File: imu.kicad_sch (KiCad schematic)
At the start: 9 parts, among them U5 MPU-6500

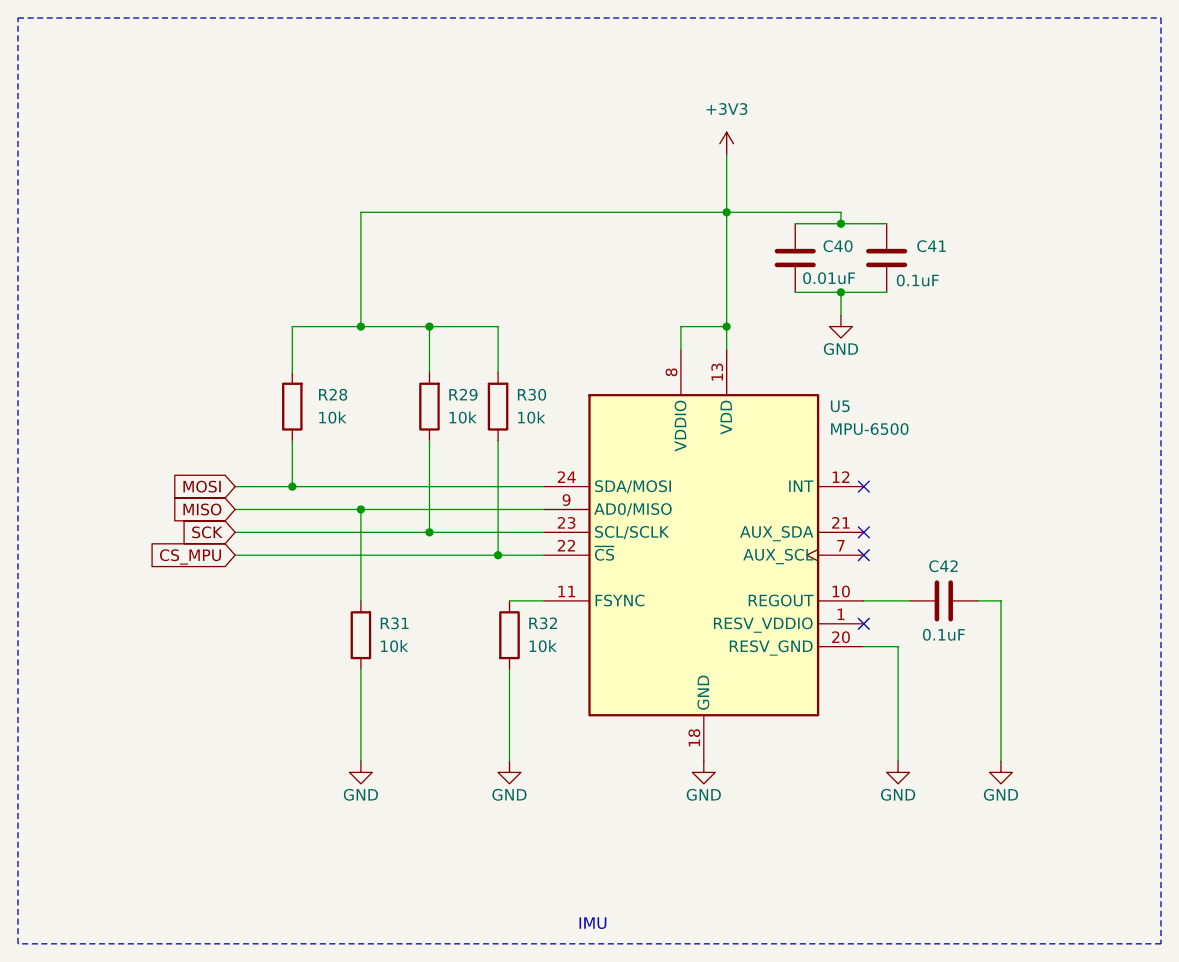
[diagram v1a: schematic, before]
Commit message: Major update on results of testing first order board and on results of crosscheck
* reworked mainswitch scheme
* mainswitch divider. expected commutation time - 2us
* added 3v3bt and 3v3hall
* tvs on hall
* divided 5vhall, 3vhall, 3vbt
* fix misplacement gnd and 3v3 at the BT connector
* fix motorbut (now pullup and gnd on button)
* fix opto gate

+ a lot of minors
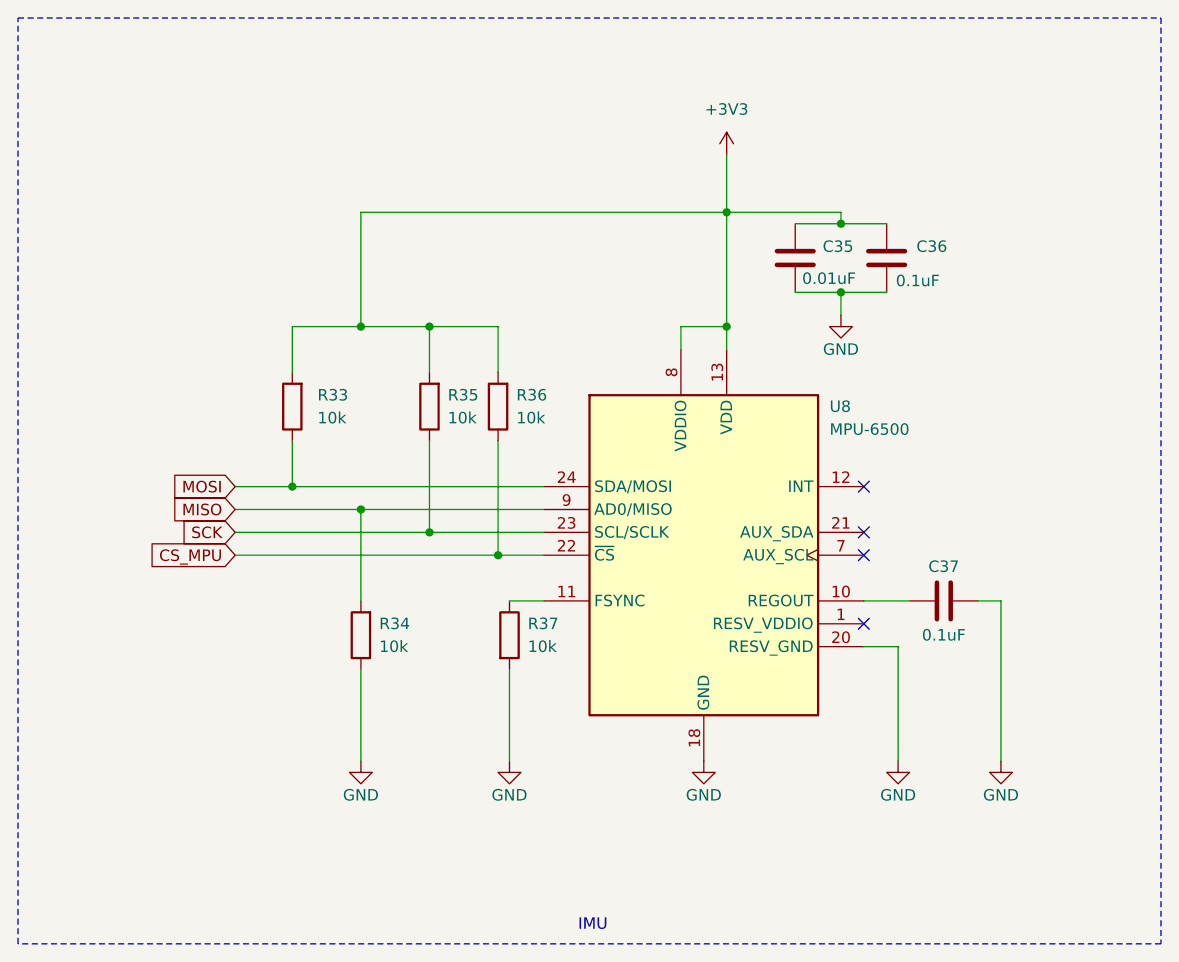
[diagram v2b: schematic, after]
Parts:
- renumbered C40 to C35, C41 to C36, C42 to C37, R28 to R33, R31 to R34, R29 to R35, R30 to R36, R32 to R37, U5 to U8
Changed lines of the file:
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@@
 		(on_board yes)
 		(dnp no)
-		(property "Reference" "R32"
+		(property "Reference" "R37"
 			(at 145.542 113.0299 0)
 			(effects
@@
 			(project "ShiftWay_f103"
 				(path "/c57bc97c-1c43-4bb1-9424-fed846030b7b/44aacc1d-3f92-4714-b852-d77f581a6611"
-					(reference "R32")
+					(reference "R37")
 					(unit 1)
 				)
@@
 		(on_board yes)
 		(dnp no)
-		(property "Reference" "#PWR074"
+		(property "Reference" "#PWR073"
 			(at 186.69 134.62 0)
 			(effects
@@
 			(project "ShiftWay_f103"
 				(path "/c57bc97c-1c43-4bb1-9424-fed846030b7b/44aacc1d-3f92-4714-b852-d77f581a6611"
-					(reference "#PWR074")
+					(reference "#PWR073")
 					(unit 1)
 				)
@@
 		(dnp no)
 		(fields_autoplaced yes)
-		(property "Reference" "#PWR069"
+		(property "Reference" "#PWR071"
 			(at 167.64 64.77 0)
 			(effects
@@
 			(project "ShiftWay_f103"
 				(path "/c57bc97c-1c43-4bb1-9424-fed846030b7b/44aacc1d-3f92-4714-b852-d77f581a6611"
-					(reference "#PWR069")
+					(reference "#PWR071")
 					(unit 1)
 				)
@@
 		(on_board yes)
 		(dnp no)
-		(property "Reference" "C41"
+		(property "Reference" "C36"
 			(at 188.722 71.1199 0)
 			(effects
@@
 			(project "ShiftWay_f103"
 				(path "/c57bc97c-1c43-4bb1-9424-fed846030b7b/44aacc1d-3f92-4714-b852-d77f581a6611"
-					(reference "C41")
+					(reference "C36")
 					(unit 1)
 				)
@@
 		(dnp no)
 		(fields_autoplaced yes)
-		(property "Reference" "R29"
+		(property "Reference" "R35"
 			(at 136.652 87.6299 0)
 			(effects
@@
 			(project "ShiftWay_f103"
 				(path "/c57bc97c-1c43-4bb1-9424-fed846030b7b/44aacc1d-3f92-4714-b852-d77f581a6611"
-					(reference "R29")
+					(reference "R35")
 					(unit 1)
 				)
@@
 		(on_board yes)
 		(dnp no)
-		(property "Reference" "#PWR073"
+		(property "Reference" "#PWR070"
 			(at 165.1 134.62 0)
 			(effects
@@
 			(project "ShiftWay_f103"
 				(path "/c57bc97c-1c43-4bb1-9424-fed846030b7b/44aacc1d-3f92-4714-b852-d77f581a6611"
-					(reference "#PWR073")
+					(reference "#PWR070")
 					(unit 1)
 				)
@@
 		(on_board yes)
 		(dnp no)
-		(property "Reference" "#PWR070"
+		(property "Reference" "#PWR072"
 			(at 180.34 85.09 0)
 			(effects
@@
 			(project "ShiftWay_f103"
 				(path "/c57bc97c-1c43-4bb1-9424-fed846030b7b/44aacc1d-3f92-4714-b852-d77f581a6611"
-					(reference "#PWR070")
+					(reference "#PWR072")
 					(unit 1)
 				)
@@
 		(on_board yes)
 		(dnp no)
-		(property "Reference" "#PWR072"
+		(property "Reference" "#PWR069"
 			(at 143.51 134.62 0)
 			(effects
@@
 			(project "ShiftWay_f103"
 				(path "/c57bc97c-1c43-4bb1-9424-fed846030b7b/44aacc1d-3f92-4714-b852-d77f581a6611"
-					(reference "#PWR072")
+					(reference "#PWR069")
 					(unit 1)
 				)
@@
 		(dnp no)
 		(fields_autoplaced yes)
-		(property "Reference" "R31"
+		(property "Reference" "R34"
 			(at 129.032 113.0299 0)
 			(effects
@@
 			(project "ShiftWay_f103"
 				(path "/c57bc97c-1c43-4bb1-9424-fed846030b7b/44aacc1d-3f92-4714-b852-d77f581a6611"
-					(reference "R31")
+					(reference "R34")
 					(unit 1)
 				)
@@
 		(dnp no)
 		(fields_autoplaced yes)
-		(property "Reference" "R28"
+		(property "Reference" "R33"
 			(at 122.174 87.6299 0)
 			(effects
@@
 			(project "ShiftWay_f103"
 				(path "/c57bc97c-1c43-4bb1-9424-fed846030b7b/44aacc1d-3f92-4714-b852-d77f581a6611"
-					(reference "R28")
+					(reference "R33")
 					(unit 1)
 				)
@@
 		(on_board yes)
 		(dnp no)
-		(property "Reference" "#PWR071"
+		(property "Reference" "#PWR068"
 			(at 127 134.62 0)
 			(effects
@@
 			(project "ShiftWay_f103"
 				(path "/c57bc97c-1c43-4bb1-9424-fed846030b7b/44aacc1d-3f92-4714-b852-d77f581a6611"
-					(reference "#PWR071")
+					(reference "#PWR068")
 					(unit 1)
 				)
@@
 		(on_board yes)
 		(dnp no)
-		(property "Reference" "#PWR075"
+		(property "Reference" "#PWR074"
 			(at 198.12 134.62 0)
 			(effects
@@
 			(project "ShiftWay_f103"
 				(path "/c57bc97c-1c43-4bb1-9424-fed846030b7b/44aacc1d-3f92-4714-b852-d77f581a6611"
-					(reference "#PWR075")
+					(reference "#PWR074")
 					(unit 1)
 				)
@@
 		(on_board yes)
 		(dnp no)
-		(property "Reference" "C42"
+		(property "Reference" "C37"
 			(at 191.77 106.68 90)
 			(effects
@@
 			(project "ShiftWay_f103"
 				(path "/c57bc97c-1c43-4bb1-9424-fed846030b7b/44aacc1d-3f92-4714-b852-d77f581a6611"
-					(reference "C42")
+					(reference "C37")
 					(unit 1)
 				)
@@
 		(dnp no)
 		(fields_autoplaced yes)
-		(property "Reference" "R30"
+		(property "Reference" "R36"
 			(at 144.272 87.6299 0)
 			(effects
@@
 			(project "ShiftWay_f103"
 				(path "/c57bc97c-1c43-4bb1-9424-fed846030b7b/44aacc1d-3f92-4714-b852-d77f581a6611"
-					(reference "R30")
+					(reference "R36")
 					(unit 1)
 				)
@@
 		(on_board yes)
 		(dnp no)
-		(property "Reference" "C40"
+		(property "Reference" "C35"
 			(at 178.308 71.1199 0)
 			(effects
@@
 			(project "ShiftWay_f103"
 				(path "/c57bc97c-1c43-4bb1-9424-fed846030b7b/44aacc1d-3f92-4714-b852-d77f581a6611"
-					(reference "C40")
+					(reference "C35")
 					(unit 1)
 				)
@@
 		(on_board yes)
 		(dnp no)
-		(property "Reference" "U5"
+		(property "Reference" "U8"
 			(at 179.07 88.9 0)
 			(effects
@@
 			(project "ShiftWay_f103"
 				(path "/c57bc97c-1c43-4bb1-9424-fed846030b7b/44aacc1d-3f92-4714-b852-d77f581a6611"
-					(reference "U5")
-					(unit 1)
-				)
+					(reference "U8")
+					(unit 1)
+				)

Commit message: Fix pullup IMU, pulldown boot0, vbat before resi
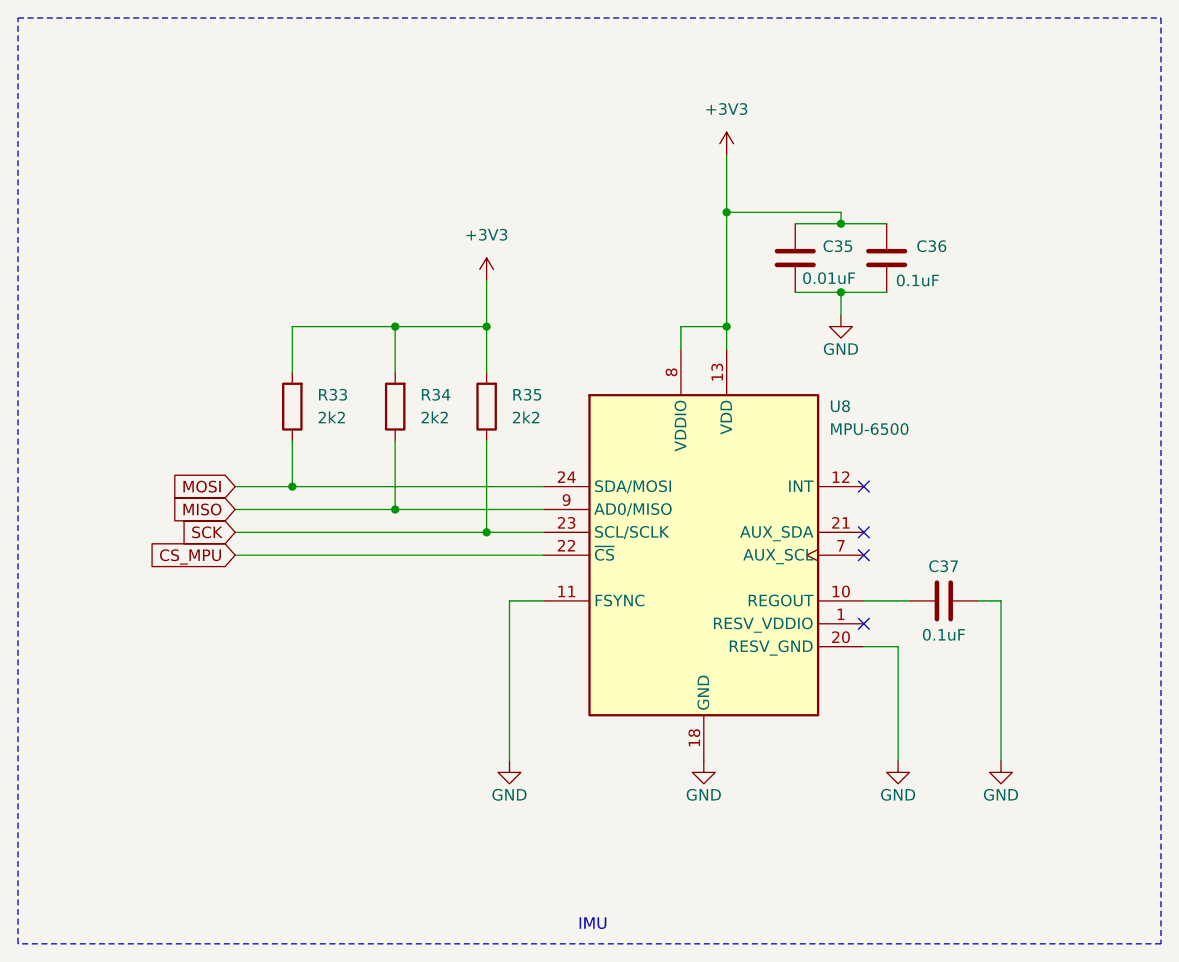
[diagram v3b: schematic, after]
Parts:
- removed R36, R37: 10k, Resistor_SMD:R_0603_1608Metric_Pad0.98x0.95mm_HandSolder, symbol Device:R
- R33, R34, R35: value 10k -> 2k2
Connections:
- net +3V3: now also R34.2
- net GND: now also U8.11 (FSYNC); no longer R34.1
- net MISO: now also R34.1; no longer R34.2
